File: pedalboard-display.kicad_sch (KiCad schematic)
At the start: 21 parts, among them J1 LED-IN, J2 LED-OUT, J3 OLED

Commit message: Fix logo
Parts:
- added SYM1: Logo_Open_Hardware_Small, Symbol:OSHW-Logo_5.7x6mm_SilkScreen, symbol Graphic:Logo_Open_Hardware_Small
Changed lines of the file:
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@@
 		(dnp no)
 		(fields_autoplaced yes)
-		(property "Reference" "#SYM1"
+		(property "Reference" "SYM1"
 			(at 270.51 147.955 0)
 			(effects
@@
 			(project ""
 				(path "/02aefeb1-bdda-4e04-a64a-6cb1fcf66702"
-					(reference "#SYM1")
+					(reference "SYM1")
 					(unit 1)
 				)

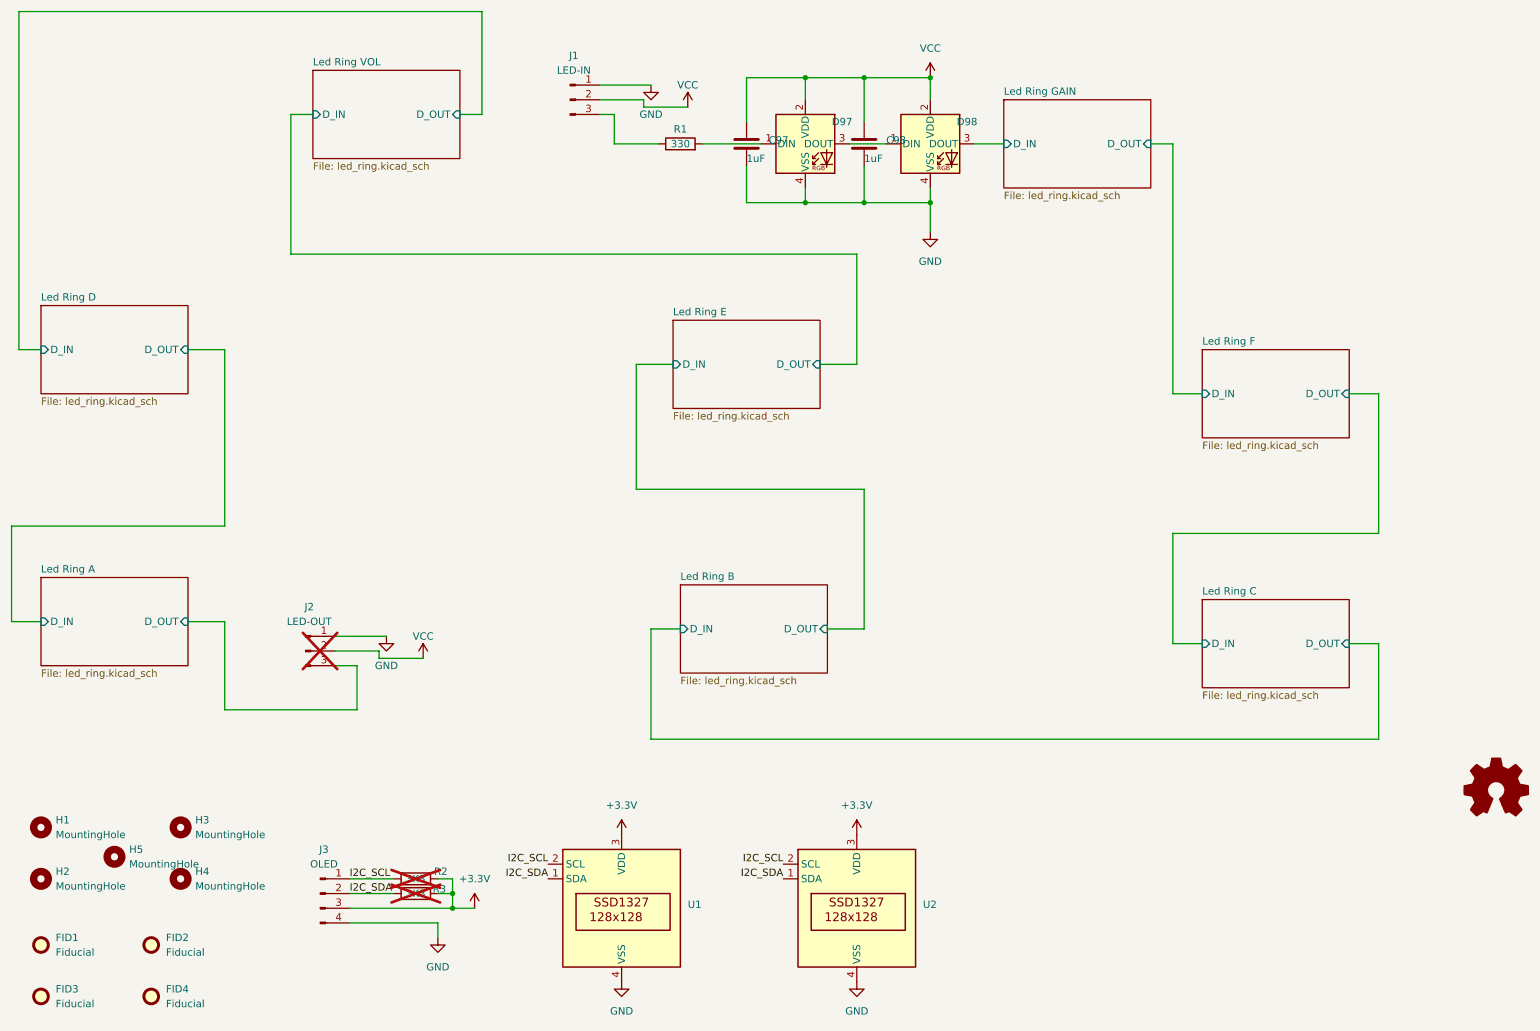
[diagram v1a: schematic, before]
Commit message: Put single leds at the end of the line
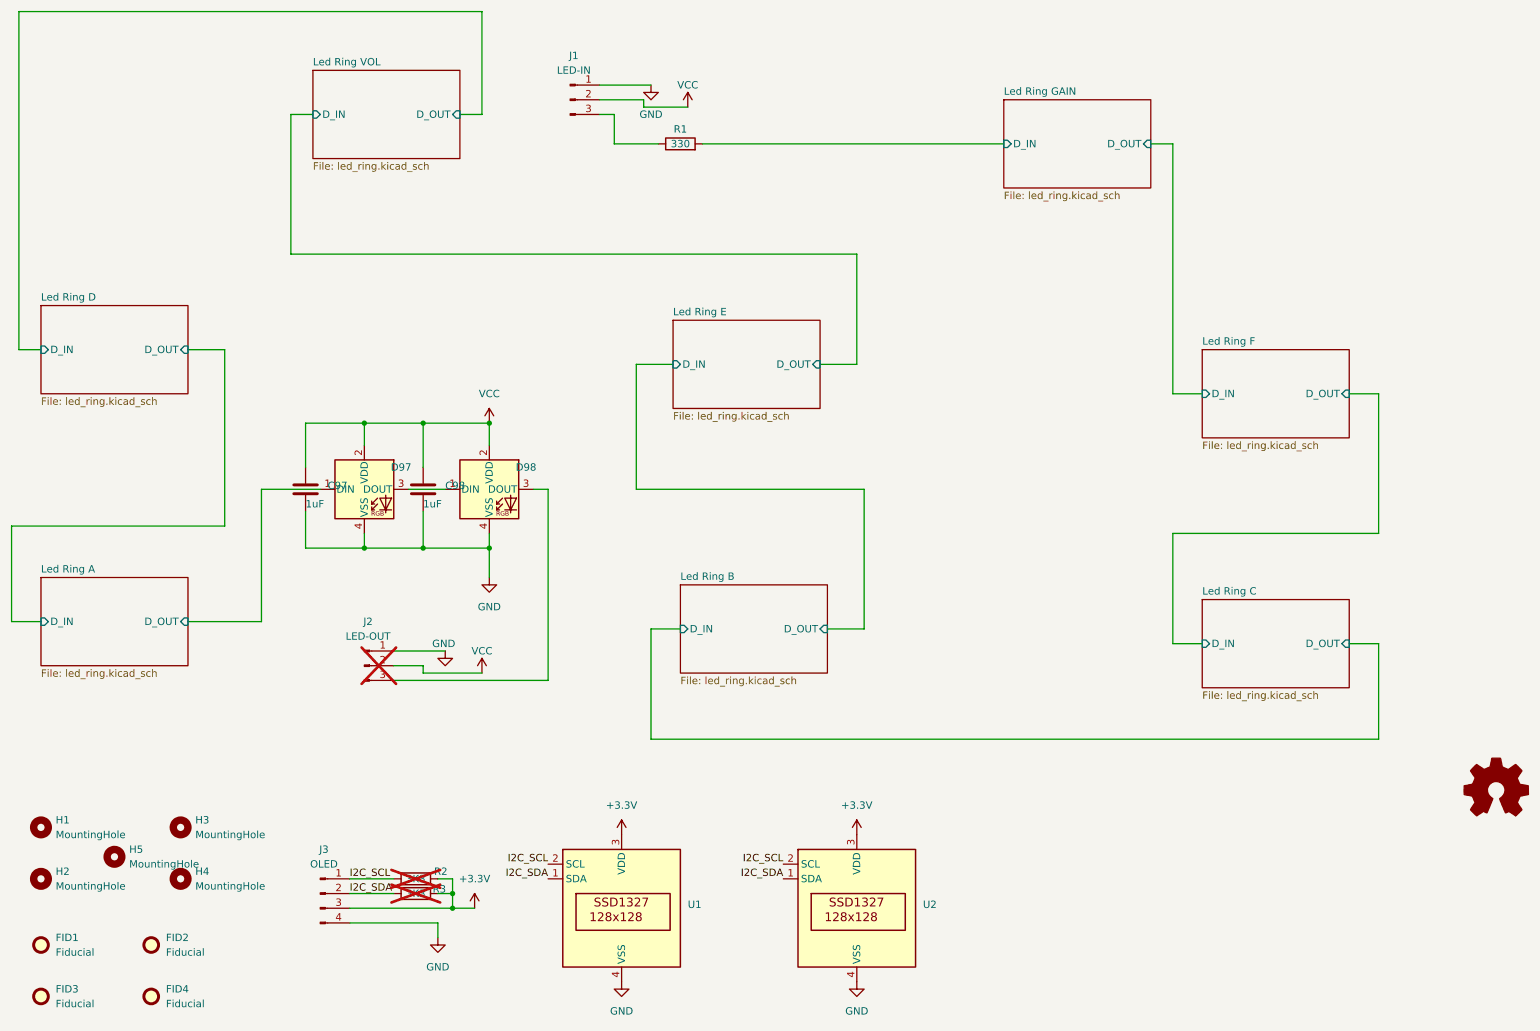
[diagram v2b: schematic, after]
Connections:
- net Led Ring A/D_OUT: now also D97.1 (DIN); no longer J2.3 (Pin_3)
- net Led Ring GAIN/D_IN: now also R1.2; no longer D98.3 (DOUT)
- new net: D98.3 (DOUT), J2.3 (Pin_3)
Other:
- moved on the sheet: C97, C98, D97, D98, J2

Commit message: Increase fiducial size
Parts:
- FID1, FID2, FID3, FID4: footprint Fiducial:Fiducial_0.5mm_Mask1mm -> Fiducial:Fiducial_1mm_Mask2mm
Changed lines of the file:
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@@
 			)
 		)
-		(property "Footprint" "Fiducial:Fiducial_0.5mm_Mask1mm"
+		(property "Footprint" "Fiducial:Fiducial_1mm_Mask2mm"
 			(at 38.1 181.61 0)
 			(effects
@@
 			)
 		)
-		(property "Footprint" "Fiducial:Fiducial_0.5mm_Mask1mm"
+		(property "Footprint" "Fiducial:Fiducial_1mm_Mask2mm"
 			(at 19.05 181.61 0)
 			(effects
@@
 			)
 		)
-		(property "Footprint" "Fiducial:Fiducial_0.5mm_Mask1mm"
+		(property "Footprint" "Fiducial:Fiducial_1mm_Mask2mm"
 			(at 38.1 190.5 0)
 			(effects
@@
 			)
 		)
-		(property "Footprint" "Fiducial:Fiducial_0.5mm_Mask1mm"
+		(property "Footprint" "Fiducial:Fiducial_1mm_Mask2mm"
 			(at 19.05 190.5 0)
 			(effects
